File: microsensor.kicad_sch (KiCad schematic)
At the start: 23 parts, among them J1 ARM SWD, Q1 TP0610T, Q2 2N7002, SW1 Control, U1 NORA B206, U2 RV-3028-C7, U3 HDC2080, Y1 32768

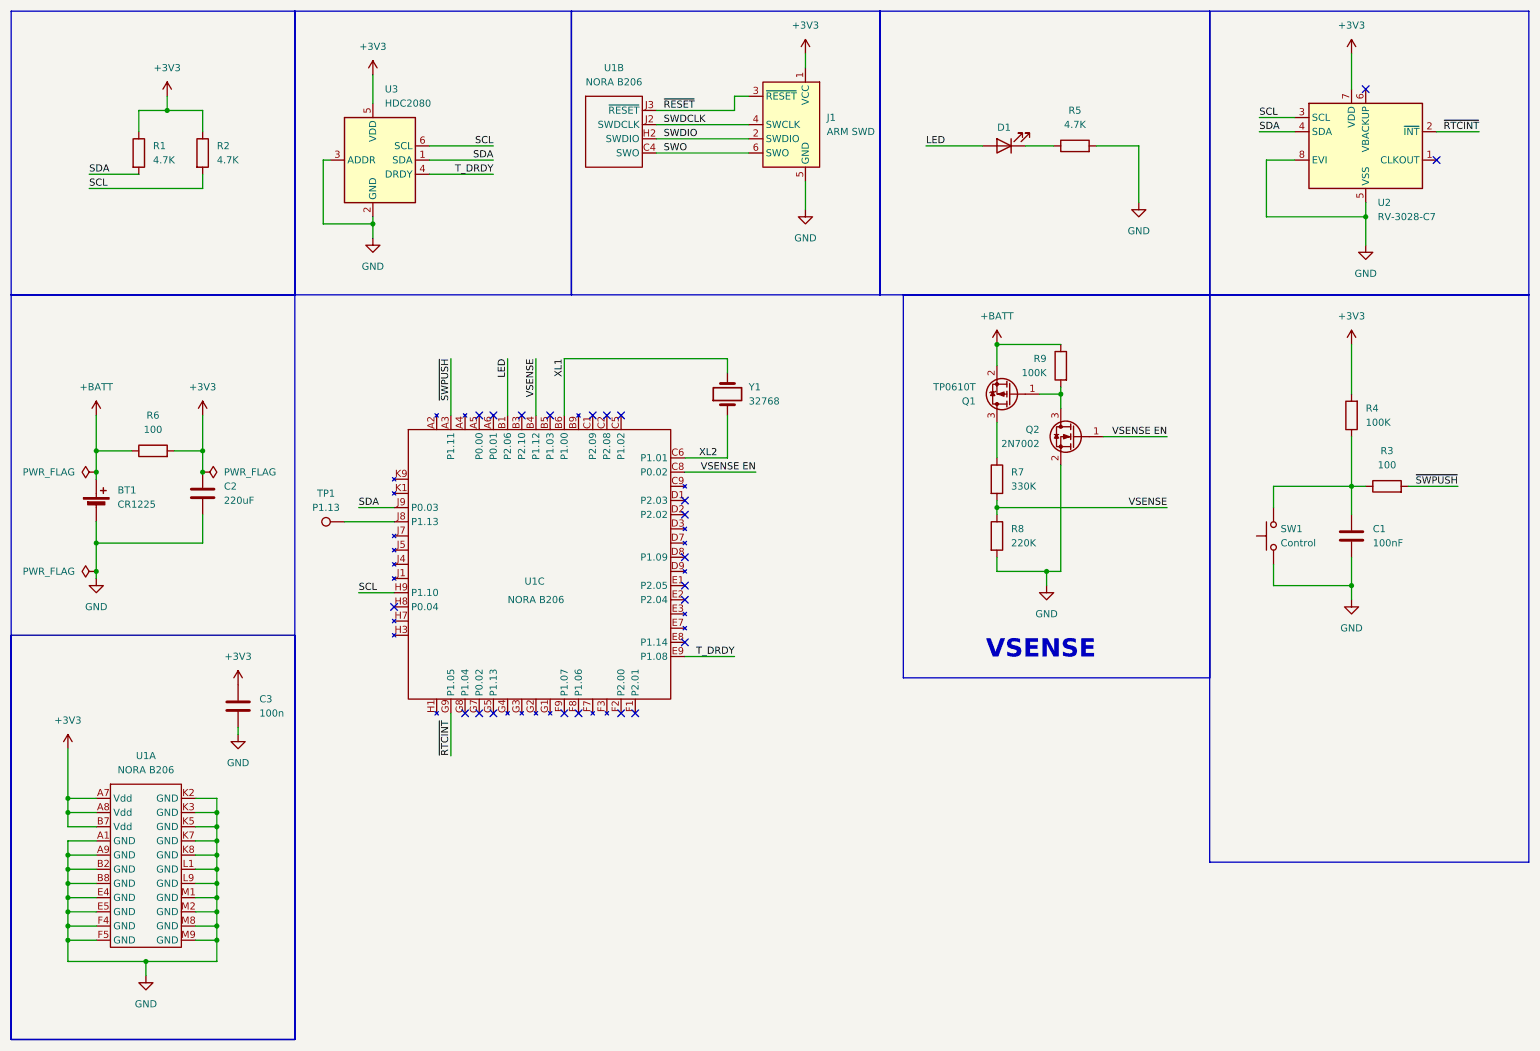
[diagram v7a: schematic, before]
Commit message: Fix I2C routed to invalid pins Remove unnecessary N-MOS Adjust placement and routing Adjust annotations (order topologically)
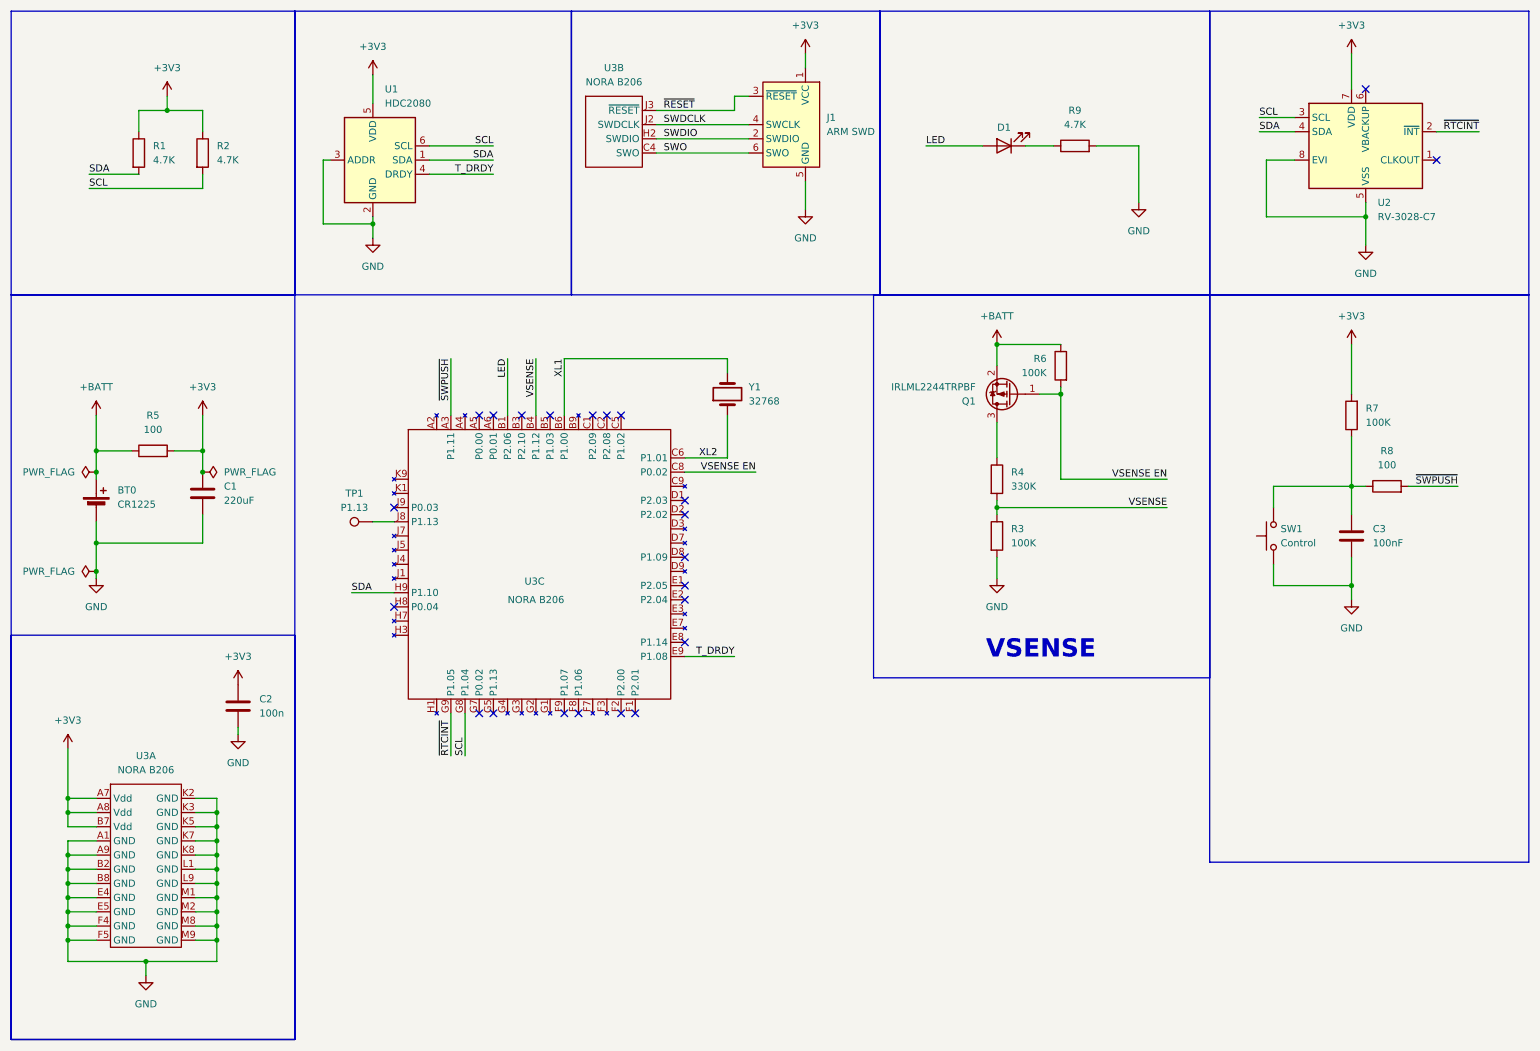
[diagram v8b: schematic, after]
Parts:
- removed Q2: 2N7002, Package_TO_SOT_SMD:SOT-23, symbol Transistor_FET:2N7002
- Q1: value TP0610T -> IRLML2244TRPBF
- R3: renamed from R8; value 220K -> 100K
- renumbered BT1 to BT0, C2 to C1, C3 to C2, C1 to C3, R7 to R4, R6 to R5, R9 to R6, R4 to R7, R3 to R8, R5 to R9, U3 to U1, U1 to U3
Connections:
- net SCL: now also U3.G8 (P1.04); no longer U3.H9 (P1.10)
- net SDA: now also U3.H9 (P1.10); no longer U3.J9 (P0.03)
- net VSENSE EN: now also Q1.1 (G), R6.2
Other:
- moved on the sheet: TP1
